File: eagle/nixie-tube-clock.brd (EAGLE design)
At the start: 156.4 x 61.9 mm, 94 parts, among them IC1 HV5622QC, IC2 HV5622QC, IC3 LM555D, IC4 MEGA8-AI, IC5 LD117ADT33TR, P1 1 k, Q1 7.3728 MHz, T1 BC547B, T2 TK3P50D, T3 BSS138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

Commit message: Replaced RGB LED + Gerber files
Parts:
- removed LED2, LED3, LED4, LED5, LED6, LED7: FYLS-5050RGBC, 00_own:6PIN_5X5MM
- added U$1, U$3, U$4, U$5, U$6, U$7: OF-SMD5060RGB, 00_own:OF-SMD5060RGB
- R16, R17, R19, R20, R22, R23, R25, R26: value 270 -> 300
- R28, R29, R31, R35: value 150 -> 300
- R30, R36: value 180 -> 330
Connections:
- net LED_B: now also U$1.B_CATH, U$3.B_CATH, U$4.B_CATH, U$5.B_CATH, U$6.B_CATH, U$7.B_CATH; no longer LED2.1_B_K, LED3.1_B_K, LED4.1_B_K, LED5.1_B_K, LED6.1_B_K, LED7.1_B_K
- net LED_G: now also U$1.G_CATH, U$3.G_CATH, U$4.G_CATH, U$5.G_CATH, U$6.G_CATH, U$7.G_CATH; no longer LED2.2_G_K, LED3.2_G_K, LED4.2_G_K, LED5.2_G_K, LED6.2_G_K, LED7.2_G_K
- net LED_R: now also U$1.R_CATH, U$3.R_CATH, U$4.R_CATH, U$5.R_CATH, U$6.R_CATH, U$7.R_CATH; no longer LED2.3_R_K, LED3.3_R_K, LED4.3_R_K, LED5.3_R_K, LED6.3_R_K, LED7.3_R_K
- net N$20: now also U$1.G_ANODE; no longer LED2.5_G_A
- net N$21: now also U$1.B_ANODE; no longer LED2.6_B_A
- net N$22: now also U$1.R_ANODE; no longer LED2.4_R_A
- net N$26: now also U$3.G_ANODE; no longer LED3.5_G_A
- net N$27: now also U$3.B_ANODE; no longer LED3.6_B_A
- net N$28: now also U$3.R_ANODE; no longer LED3.4_R_A
- net N$32: now also U$4.G_ANODE; no longer LED4.5_G_A
- net N$33: now also U$4.B_ANODE; no longer LED4.6_B_A
- net N$34: now also U$4.R_ANODE; no longer LED4.4_R_A
- net N$38: now also U$5.G_ANODE; no longer LED5.5_G_A
- net N$39: now also U$5.B_ANODE; no longer LED5.6_B_A
- net N$40: now also U$5.R_ANODE; no longer LED5.4_R_A
- net N$44: now also U$6.G_ANODE; no longer LED6.5_G_A
- net N$45: now also U$6.B_ANODE; no longer LED6.6_B_A
- net N$46: now also U$6.R_ANODE; no longer LED6.4_R_A
- net N$50: now also U$7.G_ANODE; no longer LED7.5_G_A
- net N$51: now also U$7.B_ANODE; no longer LED7.6_B_A
- net N$52: now also U$7.R_ANODE; no longer LED7.4_R_A
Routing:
- net LED_R: track 200.1 -> 235.7 mm
- net LED_G: track 217.4 -> 222.5 mm
- net N$46: track 15.3 -> 20.4 mm
- net N$40: track 16.0 -> 21.1 mm
- net N$52: track 15.3 -> 20.2 mm
- net N$28: track 15.5 -> 20.4 mm
- net N$34: track 15.1 -> 20.0 mm
- net N$22: track 15.4 -> 20.3 mm
- net N$32: track 16.9 -> 18.6 mm
- net N$50: track 16.9 -> 18.4 mm
- net N$20: track 17.0 -> 18.5 mm
- net N$44: track 17.2 -> 18.4 mm
- net N$26: track 17.3 -> 18.4 mm
- net LED_B: track 245.2 -> 246.1 mm
- net N$38: track 17.6 -> 18.5 mm

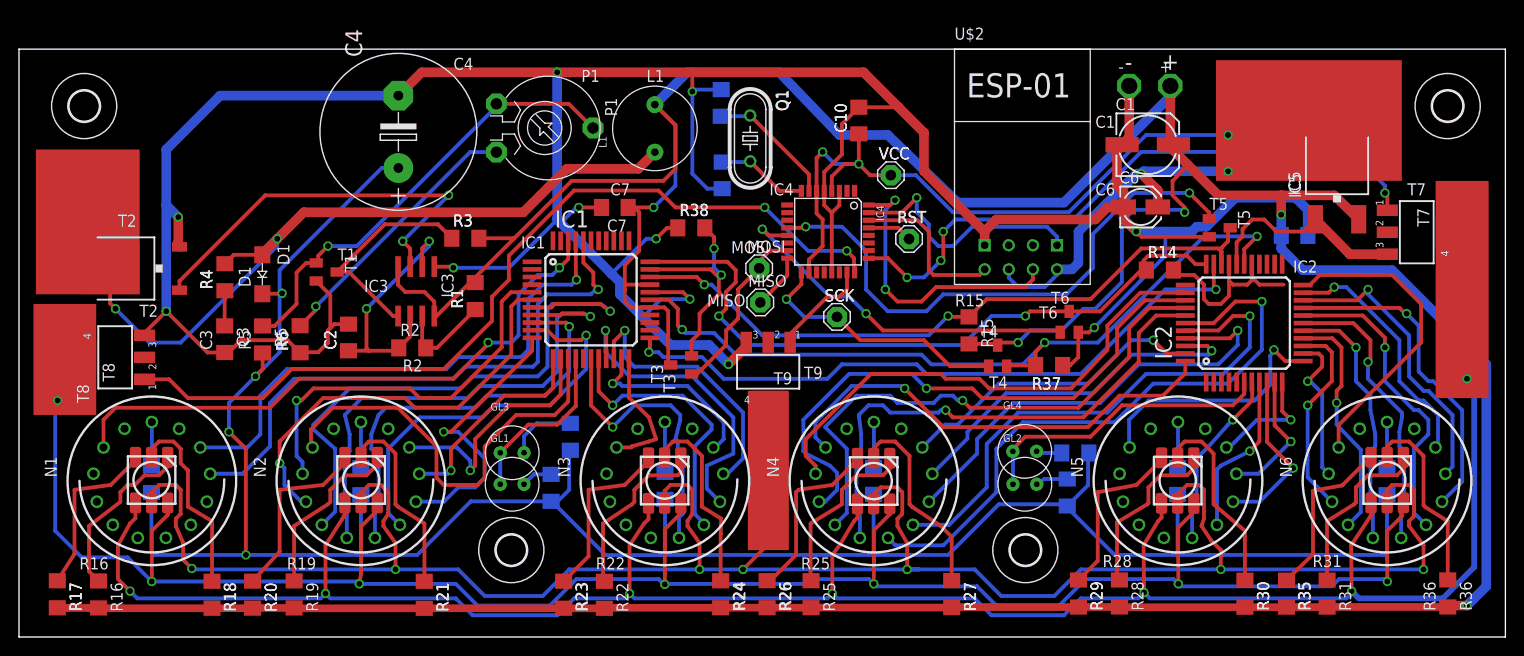
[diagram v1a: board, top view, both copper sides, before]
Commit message: Fixing GND issue at IC5 + relocation of C4, P1 and L1
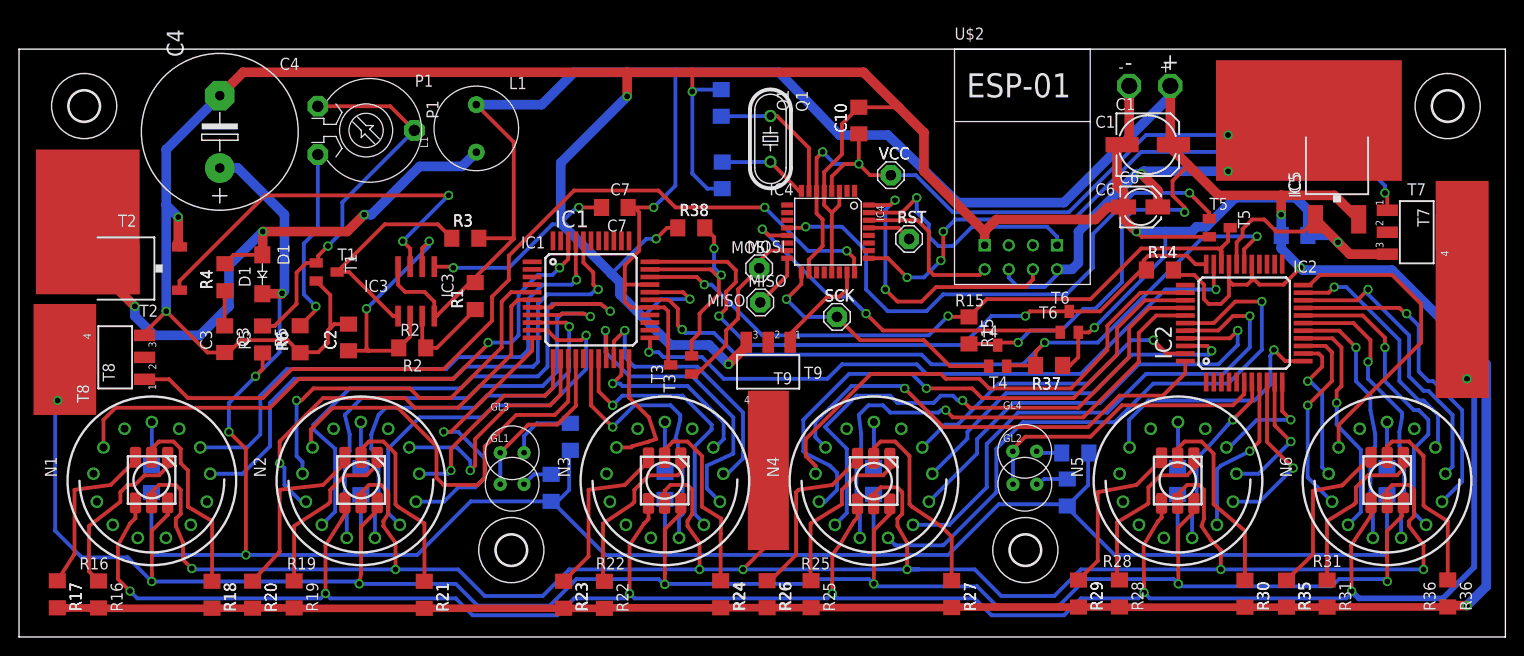
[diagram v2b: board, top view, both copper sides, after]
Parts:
- moved P1 18.8 mm to (36.5, 53.3)
- moved L1 18.8 mm to (48.1, 54.0)
- moved C4 18.8 mm to (21.1, 53.2)
- moved Q1 2.13 mm to (79.1, 52.4)
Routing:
- net N$7: track 78.1 -> 60.2 mm, vias 2 -> 3
- net +12V: track 456.6 -> 469.0 mm, vias 5 -> 6
- net N$10: track 28.5 -> 19.8 mm
- net N$8: track 47.9 -> 39.8 mm
- net GND: track 386.2 -> 393.8 mm, vias 11 -> 12
- net V+: track 246.2 -> 243.9 mm
- net N$31: track 13.6 -> 15.2 mm
- net LED_G: track 222.5 -> 223.5 mm
- net LED_D0: track 10.1 -> 10.6 mm

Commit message: Some reworks around the HV5622 ans ESP
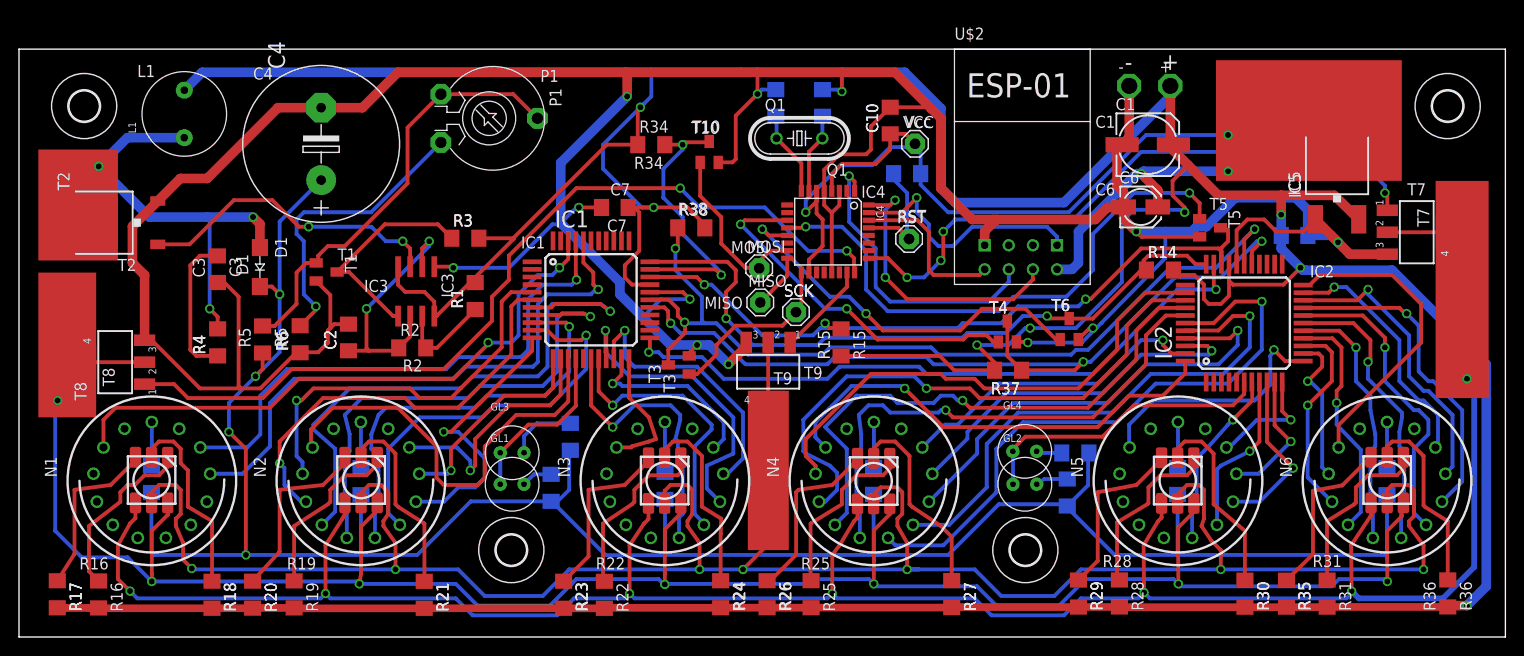
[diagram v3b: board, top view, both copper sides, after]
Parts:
- added R34, R39: 10 k, resistor:R1206
- added T10: BSS138, transistor-small-signal:SOT23
- L1: value 150 u / 1 A -> 100 u / 1 A
- R14, R15, R37, R38: value 100 k -> 10 k
- R16, R17, R19, R20, R22, R23, R25, R26, R28, R29, R31, R35: value 300 -> 470
- R18, R21, R24, R27, R30, R36: value 330 -> 510
- moved L1 30.8 mm to (17.4, 55.6)
- moved R15 13.5 mm to (86.5, 31.0)
- moved P1 13.0 mm to (49.5, 54.6)
- moved C4 10.7 mm to (31.8, 51.9)
- moved C9 10.7 mm to (84.6, 56.2)
- moved C8 9.49 mm to (79.7, 56.2), turned to 90 degrees
- moved C3 7.41 mm to (20.9, 38.7)
- moved R4 6.90 mm to (20.9, 31.0)
- moved T2 5.34 mm to (9.81, 43.6)
- moved R37 4.35 mm to (104.1, 28.1)
- moved SCK 4.35 mm to (81.8, 34.2)
- moved VCC 4.17 mm to (94.3, 51.9)
- moved C10 3.30 mm to (91.7, 54.4)
- moved Q1 3.05 mm to (82.1, 52.5), turned to 180 degrees
- moved T4 2.74 mm to (104.0, 32.2)
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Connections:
- removed net N$1: IC4.29, RST.MP
- removed net N$25: IC4.17, SCK.MP, T4.1
- new net CH_PD: IC4.1, U$2.CH_PD
- new net N$35: IC4.17, SCK.MP, T3.1
- new net N$41: IC4.15, MOSI.MP, T10.1
- new net N$43: IC4.11, T4.1
- new net POL: IC1.27, IC2.27, R37.1, T4.3
- net +12V: now also R34.2, R37.2, R38.2; no longer IC1.27, IC2.27, T3.3, T4.3
- net +3V3: now also R39.2; no longer U$2.CH_PD
- net CLK: now also R38.1, T3.3; no longer R37.2, T4.2
- net GND: now also T10.2, T3.2, T4.2; no longer R37.1, R38.1
- net MOSI: now also R34.1, T10.3; no longer R38.2, T3.2
- net N$2: now also IC4.29, R39.1, RST.MP; no longer IC4.15, MOSI.MP, T3.1
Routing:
- net POL: track 0.00 -> 89.0 mm, vias 0 -> 3
- net +12V: track 469.0 -> 522.9 mm, vias 6 -> 8
- net N$43: track 0.00 -> 37.7 mm, vias 0 -> 2
- net CH_PD: track 0.00 -> 31.4 mm, vias 0 -> 1
- net N$25: track 27.7 -> 0.00 mm, vias 1 -> 0
- net N$35: track 0.00 -> 18.9 mm
- net N$41: track 0.00 -> 18.7 mm
- net GND: track 393.8 -> 407.0 mm
- net N$9: track 3.70 -> 15.3 mm
- net N$10: track 19.8 -> 31.3 mm
- net CLK: track 82.7 -> 93.4 mm
- net N$6: track 42.8 -> 32.5 mm
- net N$7: track 60.2 -> 50.8 mm
- net N$31: track 15.2 -> 8.44 mm
- net MOSI: track 23.1 -> 29.6 mm
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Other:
- board text added: "R34"
- board text added: "R39"
- board text added: "T10"
- board text added: "Vcc"
- board text removed: "VCC"

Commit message: Final adjustments
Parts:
- moved P1 1.78 mm to (49.5, 52.8)
- moved C10 1.27 mm to (90.4, 54.4)
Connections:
- new net GLIMM_2: GL2.C, IC2.6
- new net GLIMM_3: GL4.C, IC2.5
- net GLIMM_0: now also IC1.16; no longer GL3.C, IC1.15
- net GLIMM_1: now also GL3.C, IC1.15; no longer GL2.C, GL4.C, IC2.6
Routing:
- net GLIMM_2: track 0.00 -> 29.7 mm
- net GLIMM_3: track 0.00 -> 29.3 mm
- net GLIMM_1: track 31.7 -> 15.1 mm
- net GND: track 407.0 -> 394.3 mm
- net LED_R: track 241.9 -> 235.7 mm
- net LED_G: track 229.4 -> 223.2 mm
- net LED_B: track 252.3 -> 246.1 mm
- net N$10: track 31.3 -> 27.5 mm
- net N$8: track 45.8 -> 44.0 mm
- net GLIMM_0: track 18.8 -> 17.7 mm
- net MIN_1_0: track 49.0 -> 48.3 mm
- net +3V3: track 127.3 -> 127.9 mm
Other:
- board text added: "VCC"
- board text removed: "Vcc"
